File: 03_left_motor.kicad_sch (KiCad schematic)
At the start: 9 parts, among them J4 LEFT MOTOR + ENCODER, U2 VNH5019A-E

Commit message: Correct motor cable pinout and add power solder pads
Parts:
- added J15: LEFT MOTOR LARGE SOLDER PADS, Connector_Wire:SolderWire-1.5sqmm_1x02_P7.8mm_D1.7mm_OD3.9mm, symbol Connector_Generic:Conn_01x02
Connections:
- net 3V3: now also J4.5 (Pin_5); no longer J4.4 (Pin_4)
- net GND: now also J4.2 (Pin_2); no longer J4.3 (Pin_3)
- net LEFT_ENC_A_RAW: now also J4.3 (Pin_3); no longer J4.5 (Pin_5)
- net LEFT_ENC_B_RAW: now also J4.4 (Pin_4); no longer J4.6 (Pin_6)
- net LEFT_OUTA: now also J15.1 (Pin_1)
- net LEFT_OUTB: now also J4.6 (Pin_6), J15.2 (Pin_2); no longer J4.2 (Pin_2)
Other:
- note added: "J15: large 1.7 mm through-holes in parallel with pins 1/6 for separately soldered red and white motor-power wires."
- note added: "J4/J5 cable: 1 RED motor+; 2 BLACK encoder GND; 3 YELLOW encoder A; 4 GREEN encoder B; 5 BLUE encoder +3V3; 6 WHITE motor-."
- note removed: "J connector pinout: 1 red motor A; 2 white motor B; 3 black GND; 4 blue +3V3; 5 yellow encoder A; 6 green encoder B."

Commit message: Complete pre-PCB electrical and safety audit
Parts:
- added C13: 100 nF 50 V, Capacitor_SMD:C_0805_2012Metric, symbol Device:C
- added C14: 1 uF 25 V, Capacitor_SMD:C_0805_2012Metric, symbol Device:C
- added C18: 100 nF 50 V FIT AT MOTOR, symbol Device:C
- added D17, D18: BAT54, Diode_SMD:D_SOD-323, symbol Device:D_Schottky
- added F5: 5 A MINI BLADE MOTOR BRANCH, Fuse:Fuseholder_Blade_Mini_Keystone_3568, symbol Device:Fuse
- added R84, R85: 10 k pulldown, Resistor_SMD:R_0805_2012Metric, symbol Device:R
- added R86: 10 k fault pullup, Resistor_SMD:R_0805_2012Metric, symbol Device:R
- added R88: 4.7 k ADC protect, Resistor_SMD:R_0805_2012Metric, symbol Device:R
- added R89: 1 k diag series, Resistor_SMD:R_0805_2012Metric, symbol Device:R
- added TP20: VBAT, TestPoint:TestPoint_Loop_D2.50mm_Drill1.0mm, symbol Connector:TestPoint
- added TP21: PWM, TestPoint:TestPoint_Loop_D2.50mm_Drill1.0mm, symbol Connector:TestPoint
- added TP22: INA, TestPoint:TestPoint_Loop_D2.50mm_Drill1.0mm, symbol Connector:TestPoint
- added TP23: INB, TestPoint:TestPoint_Loop_D2.50mm_Drill1.0mm, symbol Connector:TestPoint
- added TP24: DIAG, TestPoint:TestPoint_Loop_D2.50mm_Drill1.0mm, symbol Connector:TestPoint
- added TP25: CS ADC, TestPoint:TestPoint_Loop_D2.50mm_Drill1.0mm, symbol Connector:TestPoint
- added TP26: ENC A, TestPoint:TestPoint_Loop_D2.50mm_Drill1.0mm, symbol Connector:TestPoint
- added TP27: ENC B, TestPoint:TestPoint_Loop_D2.50mm_Drill1.0mm, symbol Connector:TestPoint
- added TP28: GND, TestPoint:TestPoint_Loop_D2.50mm_Drill1.0mm, symbol Connector:TestPoint
- C12: value 470 uF 25 V -> 470 uF 35 V LOW ESR
- R7: value 1 k current sense -> 680 R current sense
- R80, R81, R82: value 100 k pulldown -> 1 k series
- R83: value 10 k fault pullup -> 10 k pulldown
- U2: footprint Package_SO:ST_MultiPowerSO-30 -> PickleballRobot:VNH5019_MultiPowerSO30_ThermalVias
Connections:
- net 3V3: now also D18.2 (A), R86.2; no longer J4.5 (Pin_5), R83.2
- net GND: now also R83.2, C13.2, C14.2, D17.1 (K), R84.2, R85.2, TP28.1; no longer R80.2, R81.2, R82.2
- net GPIO25_L_PWM: no longer U2.7 (PWM)
- net GPIO26_L_INA: no longer U2.4 (INA)
- net GPIO27_L_INB: no longer U2.10 (INB)
- net LEFT_OUTA: now also C18.1
- net LEFT_OUTB: now also C18.2
- net SENSOR_VP_GPIO36: now also D17.2 (A), D18.1 (K), R88.2, TP25.1; no longer R7.1, U2.8 (CS)
- net LEFT_ENC_A_RAW renamed LEFT_ENC_A_CABLE
- net LEFT_ENC_A_CABLE: now also TP26.1
- net LEFT_ENC_B_RAW renamed LEFT_ENC_B_CABLE
- net LEFT_ENC_B_CABLE: now also TP27.1
- net MOTOR_DIAG renamed LEFT_DIAG
- net LEFT_DIAG: now also R86.1, R89.1, TP24.1; no longer R83.1
- net VBAT_SW renamed LEFT_VBAT
- net LEFT_VBAT: now also C13.1, C14.1, F5.2, TP20.1
- new net ACT_VBAT: F5.1
- new net ENC_3V3: J4.5 (Pin_5)
- new net GPIO23_LEFT_DIAG: R89.2
- new net LEFT_CS_RAW: R7.1, R88.1, U2.8 (CS)
- new net LEFT_INA_DRV: R81.2, R84.1, TP22.1, U2.4 (INA)
- new net LEFT_INB_DRV: R82.2, R85.1, TP23.1, U2.10 (INB)
- new net LEFT_PWM_DRV: R80.2, R83.1, TP21.1, U2.7 (PWM)

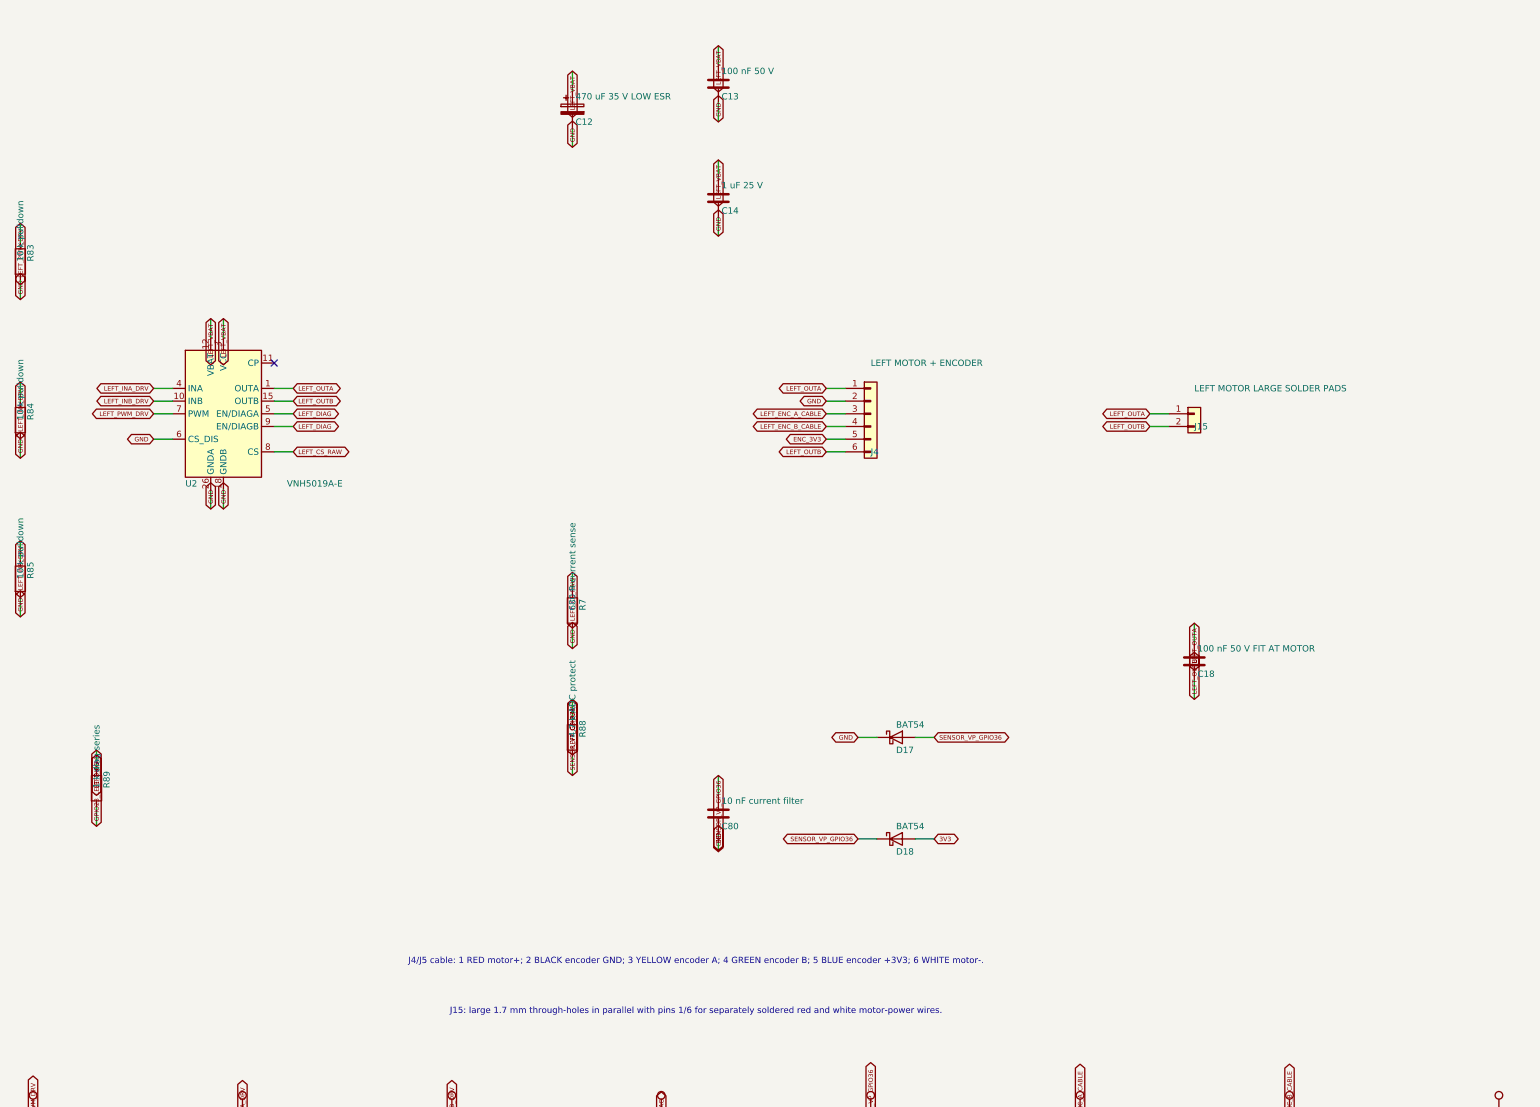
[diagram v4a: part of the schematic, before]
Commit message: Correct critical controller schematic safety issues
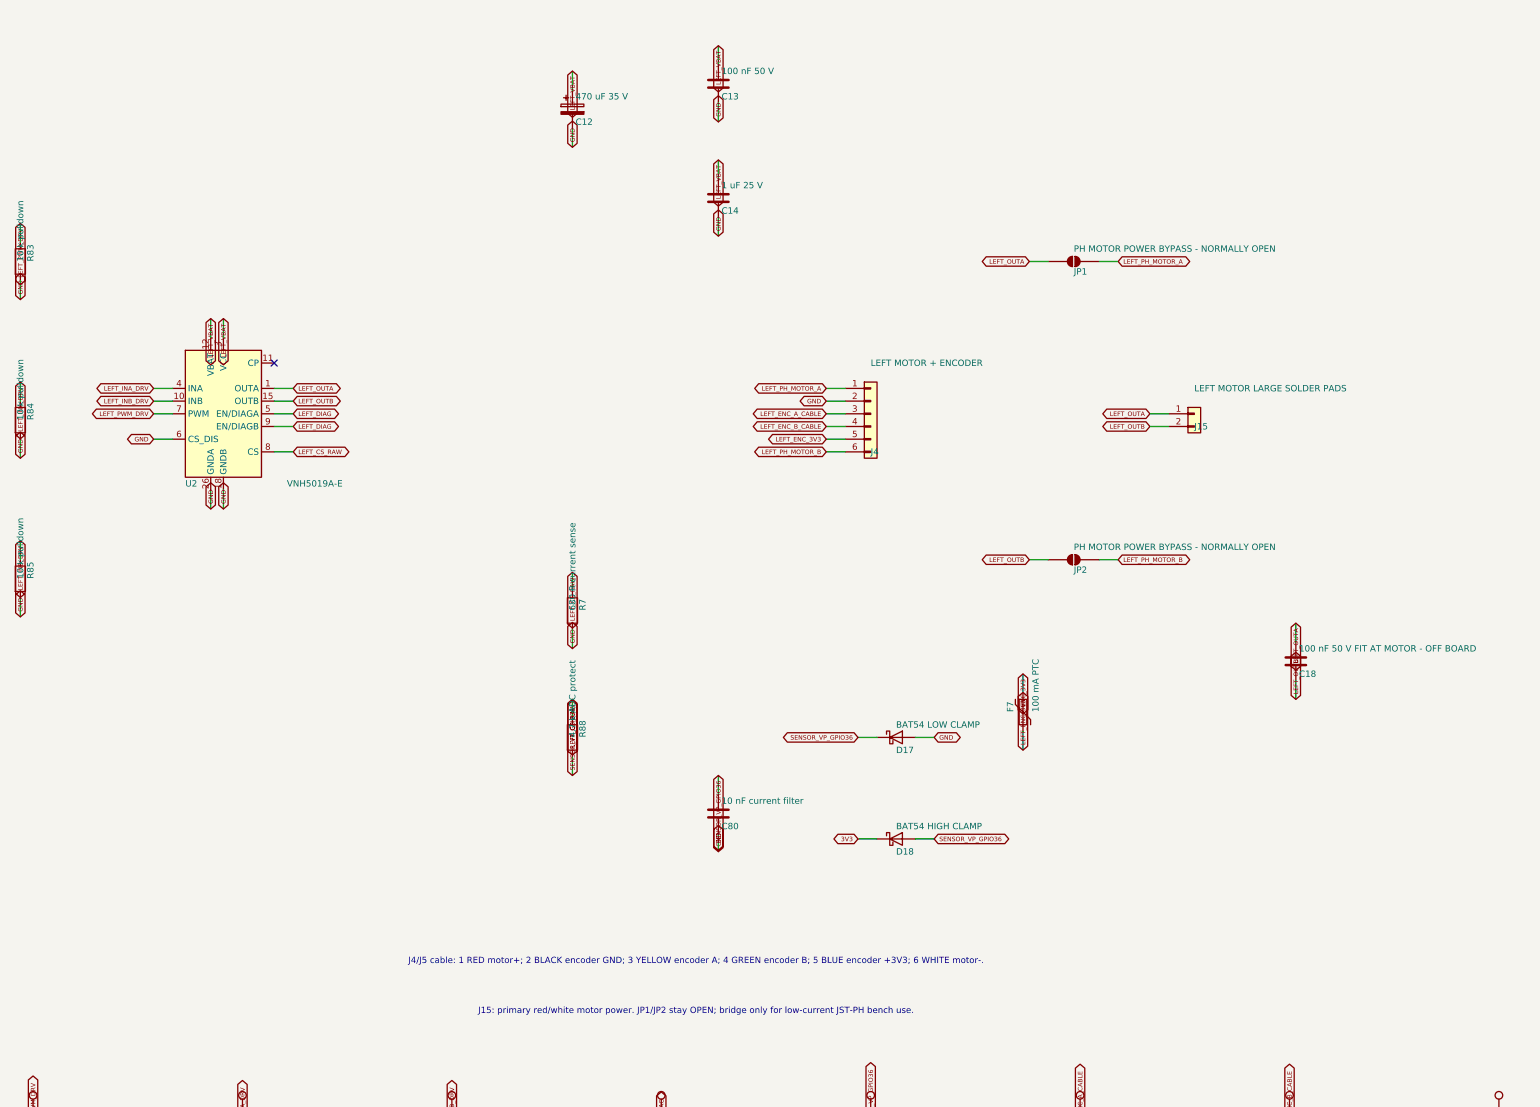
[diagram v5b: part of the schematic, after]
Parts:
- removed R89: 1 k diag series, Resistor_SMD:R_0805_2012Metric, symbol Device:R
- added F7: 100 mA PTC, Fuse:Fuse_0805_2012Metric, symbol Device:Polyfuse
- added JP1, JP2: PH MOTOR POWER BYPASS - NORMALLY OPEN, Jumper:SolderJumper-2_P1.3mm_Open_Pad1.0x1.5mm, symbol Jumper:SolderJumper_2_Open
- C12: value 470 uF 35 V LOW ESR -> 470 uF 35 V; footprint Capacitor_THT:CP_Radial_D8.0mm_P3.50mm -> Capacitor_THT:CP_Radial_D10.0mm_P5.00mm
- C18: value 100 nF 50 V FIT AT MOTOR -> 100 nF 50 V FIT AT MOTOR - OFF BOARD
- D17: value BAT54 -> BAT54 LOW CLAMP
- D18: value BAT54 -> BAT54 HIGH CLAMP
- TP20, TP21, TP22, TP23, TP24, TP25, TP26, TP27, TP28: footprint TestPoint:TestPoint_Loop_D2.50mm_Drill1.0mm -> TestPoint:TestPoint_Pad_D1.5mm; now left out of the parts list
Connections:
- net 3V3: now also D18.1 (K); no longer D18.2 (A)
- net ENC_3V3: now also F7.1; no longer J4.5 (Pin_5)
- net GND: now also D17.2 (A); no longer D17.1 (K)
- net LEFT_OUTA: now also JP1.1 (A); no longer J4.1 (Pin_1)
- net LEFT_OUTB: now also JP2.1 (A); no longer J4.6 (Pin_6)
- net SENSOR_VP_GPIO36: now also D17.1 (K), D18.2 (A); no longer D17.2 (A), D18.1 (K)
- new net LEFT_ENC_3V3: F7.2, J4.5 (Pin_5)
- new net LEFT_PH_MOTOR_A: J4.1 (Pin_1), JP1.2 (B)
- new net LEFT_PH_MOTOR_B: J4.6 (Pin_6), JP2.2 (B)
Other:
- note added: "J15: primary red/white motor power. JP1/JP2 stay OPEN; bridge only for low-current JST-PH bench use."
- note removed: "J15: large 1.7 mm through-holes in parallel with pins 1/6 for separately soldered red and white motor-power wires."
